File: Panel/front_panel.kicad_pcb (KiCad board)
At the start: 4 copper layers, 0 parts

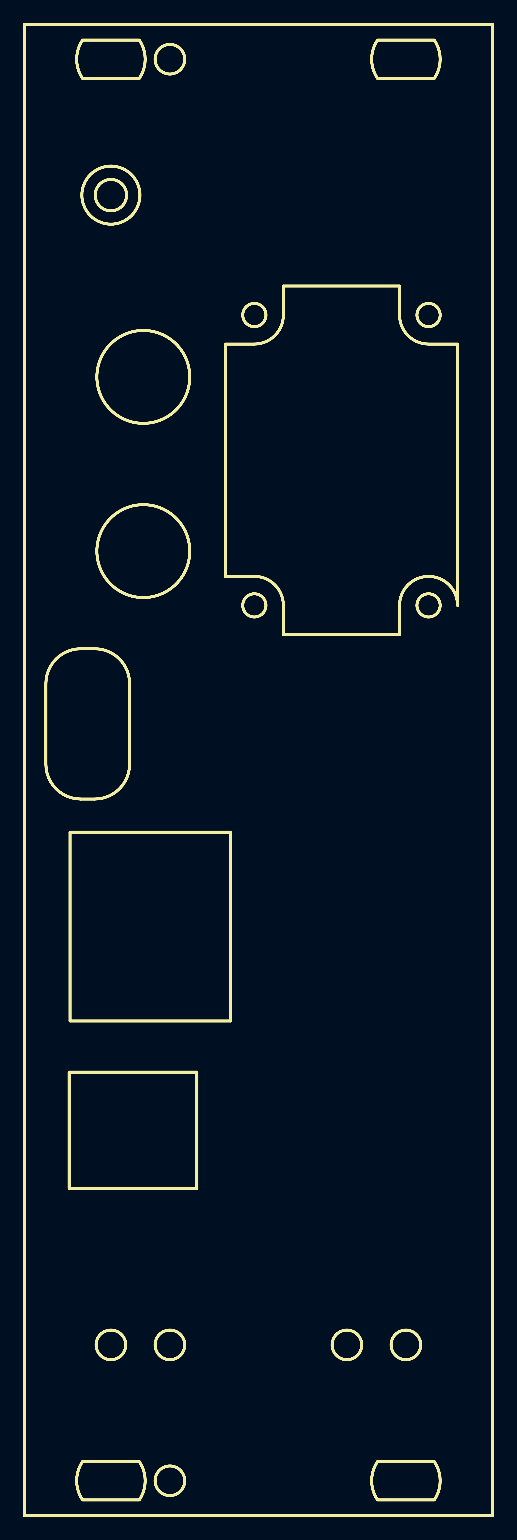
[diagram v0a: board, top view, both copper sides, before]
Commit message: Front Panel: Relocate markings to diff layers - Move the markings to different layers for generating prod docs - Add comments in the drawings pdf
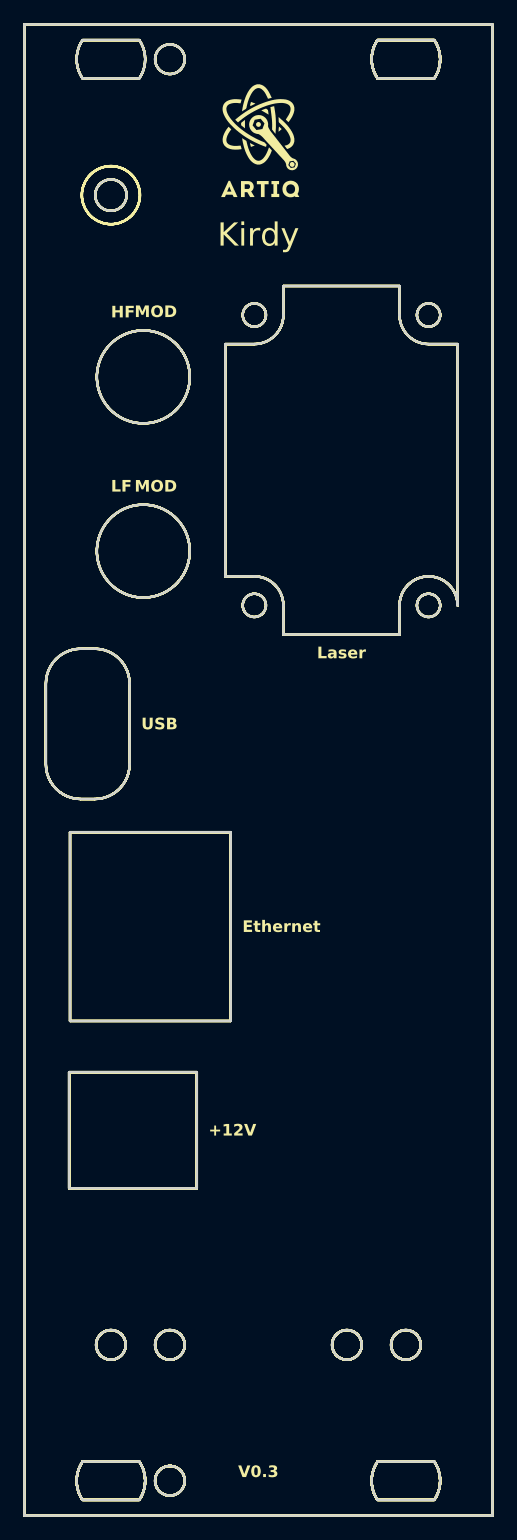
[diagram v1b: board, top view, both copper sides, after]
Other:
- board outline added: 40.3 x 128.4 mm
- board text added: "For M2.5 Raised Pozidrive Countersunk Head Reference Screw P/N: nVent SCHROFF 21100-429"
- board text added: "Front Panel Kit P/N Reference: nVent SCHROFF 20848-668"
- board text added: "List of Production Files: 3D Image of the Panel -> front_panel.png F.Silkscreen + User.2 = drawings.pdf F.Fab: Text Markings -> markings.dxf Edge_Cut + User.3: Mechanical Holes Cutout -> front_panel.dxf"
- board text added: "V0.3"
- board text removed: "F.Silkscreen: Front Panel 3D Model Outline F.Fab: Markings"
- board text removed: "V0.1"
